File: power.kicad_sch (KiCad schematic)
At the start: 7 parts, among them J5 Conn_01x02, U1 MIC5365-2.8YC5

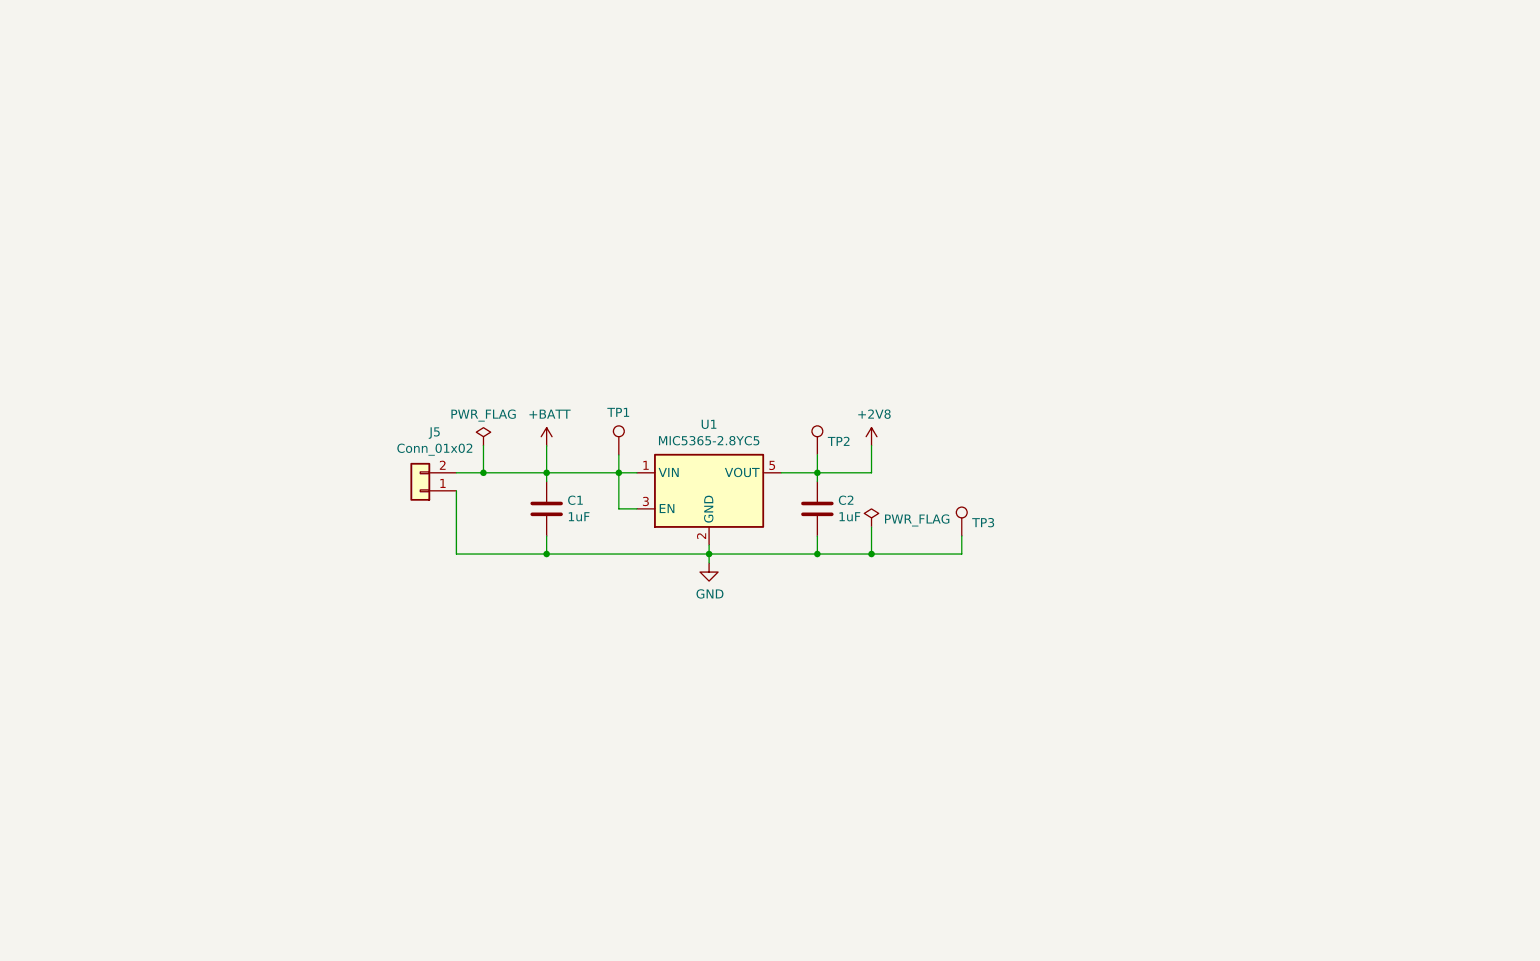
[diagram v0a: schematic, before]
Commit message: Initial schematic version
This is now a clean and ready version of the schematic:
That means:
- Schematic has been reviewed,
- It's fully annotated,
- All elements have been checked for availability with JLCPCB,
- Footprints were assigned,
- ERC is green.

No design changes should be added for this version until
the PCB is present and version is released.
Only bugfixes are possible now.
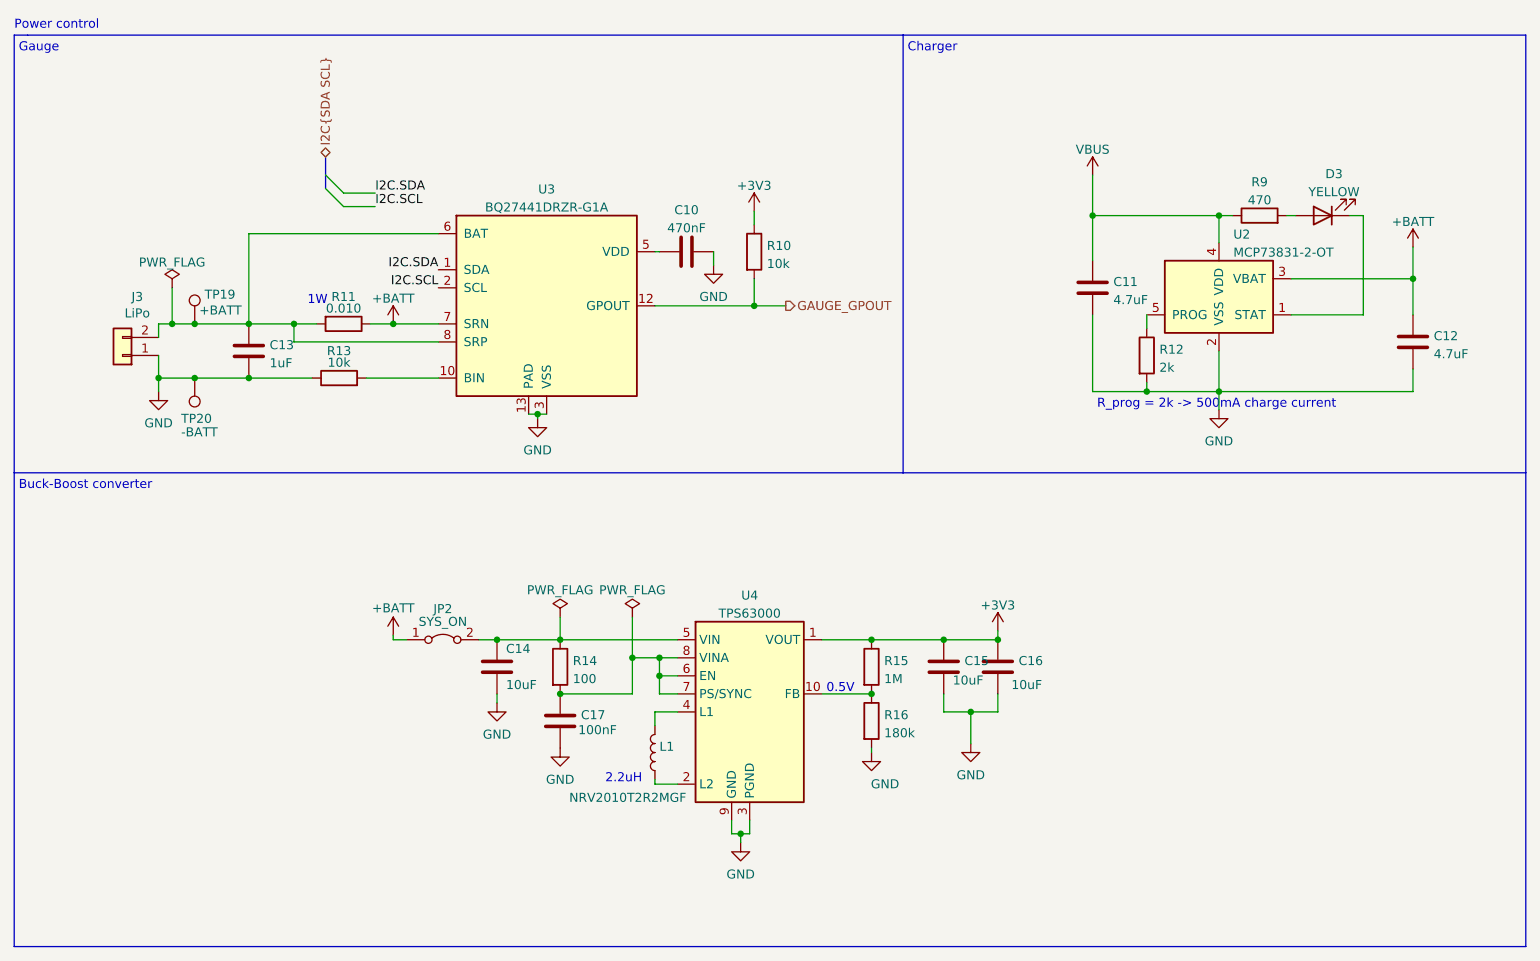
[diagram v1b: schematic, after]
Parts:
- removed C1, C2: 1uF, Capacitor_SMD:C_0402_1005Metric, symbol Device:C
- removed TP1, TP2, TP3: TestPoint, TestPoint:TestPoint_Pad_D2.0mm, symbol Connector:TestPoint
- removed U1: MIC5365-2.8YC5, Package_TO_SOT_SMD:SOT-353_SC-70-5, symbol cutomLDO:MIC5365-2.8YC5
- added C10: 470nF, Capacitor_SMD:C_0402_1005Metric, symbol Device:C
- added C11, C12: 4.7uF, Capacitor_SMD:C_0402_1005Metric, symbol Device:C
- added C13: 1uF, Capacitor_SMD:C_0402_1005Metric, symbol Device:C
- added C14, C15, C16: 10uF, Capacitor_SMD:C_0402_1005Metric, symbol Device:C
- added C17: 100nF, Capacitor_SMD:C_0402_1005Metric, symbol Device:C
- added D3: YELLOW, LED_SMD:LED_0402_1005Metric, symbol Device:LED
- added JP2: SYS_ON, Connector_PinHeader_2.54mm:PinHeader_1x02_P2.54mm_Vertical, symbol Jumper:Jumper_2_Bridged
- added L1: NRV2010T2R2MGF, Inductor_SMD:L_Taiyo-Yuden_NR-20xx, symbol Device:L
- added R10, R13: 10k, Resistor_SMD:R_0402_1005Metric, symbol Device:R
- added R11: 0.010, Resistor_SMD:R_2010_5025Metric, symbol Device:R
- added R12: 2k, Resistor_SMD:R_0402_1005Metric, symbol Device:R
- added R14: 100, Resistor_SMD:R_0402_1005Metric, symbol Device:R
- added R15: 1M, Resistor_SMD:R_0402_1005Metric, symbol Device:R
- added R16: 180k, Resistor_SMD:R_0402_1005Metric, symbol Device:R
- added R9: 470, Resistor_SMD:R_0402_1005Metric, symbol Device:R
- added TP19: +BATT, TestPoint:TestPoint_Pad_2.0x2.0mm, symbol Connector:TestPoint
- added TP20: -BATT, TestPoint:TestPoint_Pad_2.0x2.0mm, symbol Connector:TestPoint
- added U2: MCP73831-2-OT, Package_TO_SOT_SMD:SOT-23-5, symbol Battery_Management:MCP73831-2-OT
- added U3: BQ27441DRZR-G1A, Package_SON:Texas_S-PDSO-N12, symbol Battery_Management:BQ27441DRZR-G1A
- added U4: TPS63000, Package_SON:Texas_DRC0010J_ThermalVias, symbol Regulator_Switching:TPS63000
- J3: renamed from J5; value Conn_01x02 -> LiPo; footprint Connector_PinSocket_2.54mm:PinSocket_1x02_P2.54mm_Vertical -> Connector_PinHeader_2.54mm:PinHeader_1x02_P2.54mm_Vertical
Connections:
- net +BATT: now also C12.1, JP2.1 (A), R11.1, U2.3 (VBAT), U3.7 (SRN); no longer J3.2 (Pin_2)
- net GND: now also C10.2, C11.2, C12.2, C13.2, C14.2, C15.2, C16.2, C17.2, R12.2, R13.1, R16.2, TP20.1, U2.2 (VSS), U3.13 (PAD), U3.3 (VSS), U4.11 (PGND), U4.3 (PGND), U4.9 (GND)
- new net: C13.1, J3.2 (Pin_2), R11.2, TP19.1, U3.6 (BAT), U3.8 (SRP)
- new net: D3.2 (A), R9.2
- new net: L1.1, U4.2 (L2)
- new net: L1.2, U4.4 (L1)
- new net: C14.1, JP2.2 (B), R14.1, U4.5 (VIN)
- new net: C17.1, R14.2, U4.6 (EN), U4.7 (PS/SYNC), U4.8 (VINA)
- new net: R13.2, U3.10 (BIN)
- new net: D3.1 (K), U2.1 (STAT)
- new net: R12.1, U2.5 (PROG)
- new net: R15.2, R16.1, U4.10 (FB)
- new net: C10.1, U3.5 (VDD)
- new net +3V3: C15.1, C16.1, R10.1, R15.1, U4.1 (VOUT)
- new net GAUGE_GPOUT: R10.2, U3.12 (GPOUT)
- new net I2C.SCL: U3.2 (SCL)
- new net I2C.SDA: U3.1 (SDA)
- new net VBUS: C11.1, R9.1, U2.4 (VDD)
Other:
- note added: "0.5V"
- note added: "1W"
- note added: "2.2uH"
- note added: "Buck-Boost converter"
- note added: "Charger"
- note added: "Gauge"
- note added: "Power control"
- note added: "R_prog = 2k -> 500mA charge current"
- moved on the sheet: J3

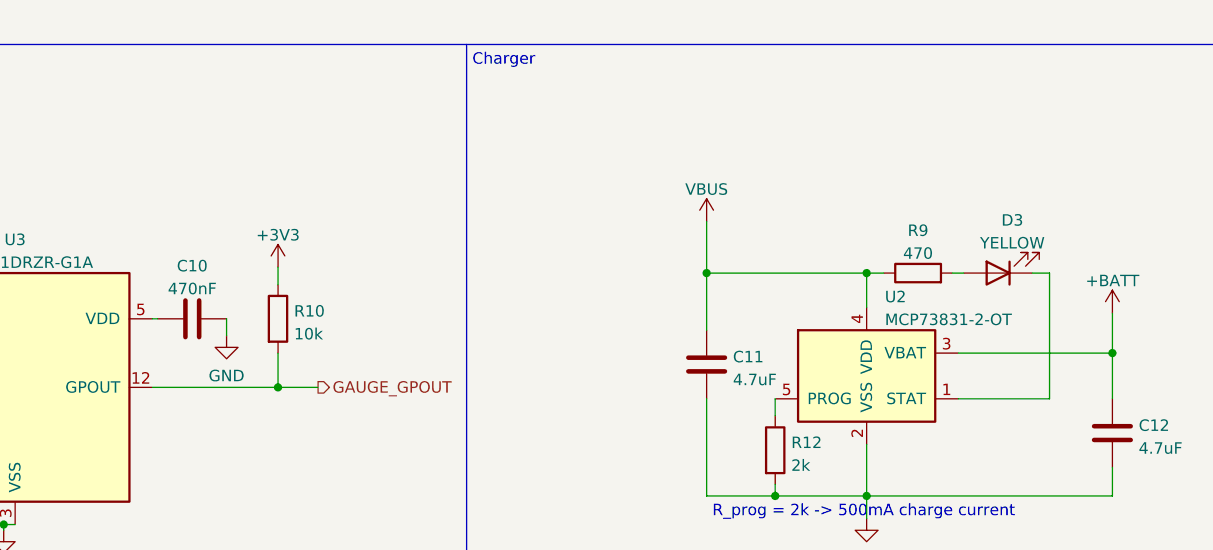
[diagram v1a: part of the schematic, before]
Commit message: Update footprints and add JLCPCB fields
Update some footprints which will suit better building the pcb
with JLCBPCB. Add fields to components sourced from JLCPCB
to be able to generate BOM.
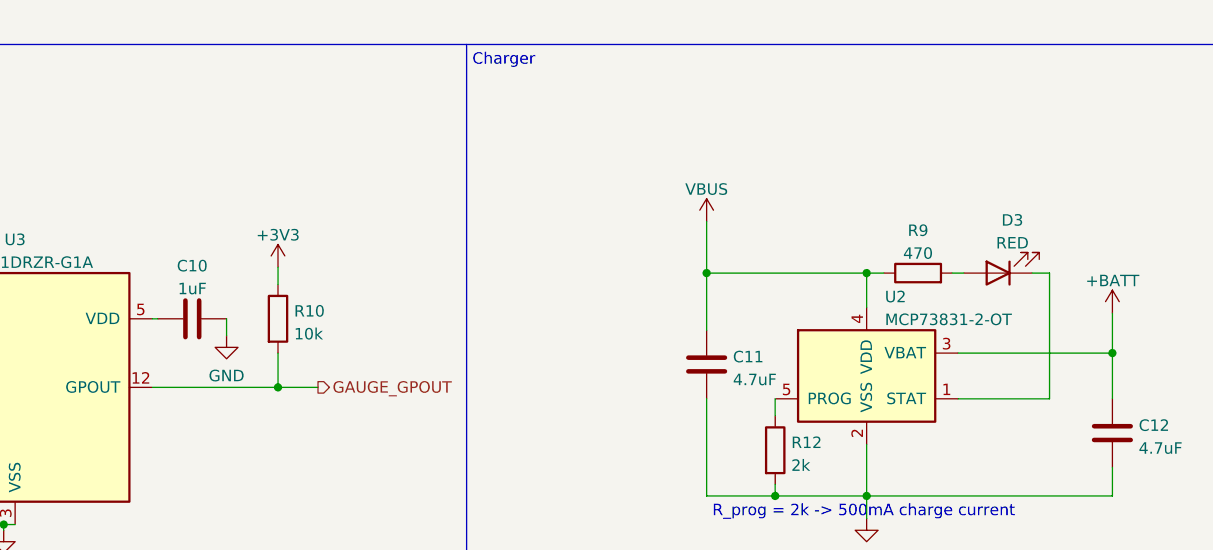
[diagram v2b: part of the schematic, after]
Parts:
- C10: value 470nF -> 1uF; JLC (none) -> 0402; LCSC (none) -> C52923
- C11, C12: JLC (none) -> 0402; LCSC (none) -> C23733
- C13: JLC (none) -> 0402; LCSC (none) -> C52923
- C14, C15, C16: JLC (none) -> 0402; LCSC (none) -> C15525
- C17: JLC (none) -> 0402; LCSC (none) -> C1525
- D3: value YELLOW -> RED; footprint LED_SMD:LED_0402_1005Metric -> LED_SMD:LED_0603_1608Metric; JLC (none) -> 0603; LCSC (none) -> C2286
- L1: JLC (none) -> SMD; LCSC (none) -> C222837
- R10, R13: JLC (none) -> 0402; LCSC (none) -> C25744
- R11: JLC (none) -> 2010; LCSC (none) -> C175965
- R12: JLC (none) -> 0402; LCSC (none) -> C4109
- R14: JLC (none) -> 0402; LCSC (none) -> C25076
- R15: JLC (none) -> 0402; LCSC (none) -> C26083
- R16: JLC (none) -> 0402; LCSC (none) -> C25760
- R9: JLC (none) -> 0402; LCSC (none) -> C25117
- U2: JLC (none) -> SOT-23-5; LCSC (none) -> C424093
- U3: JLC (none) -> SON-12-EP(2.5x4); LCSC (none) -> C473397
- U4: JLC (none) -> SON-10-EP(3.1x3.1); LCSC (none) -> C24966
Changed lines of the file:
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@@
+      (effects (font (size 1.27 1.27)) hide)
+    )
+    (property "JLC" "0402" (id 4) (at 209.55 57.785 0)
+      (effects (font (size 1.27 1.27)) hide)
+    )
+    (property "LCSC" "C25117" (id 5) (at 209.55 57.785 0)
       (effects (font (size 1.27 1.27)) hide)
     )
@@
       (effects (font (size 1.27 1.27)) hide)
     )
+    (property "JLC" "SMD" (id 4) (at 124.46 133.35 0)
+      (effects (font (size 1.27 1.27)) hide)
+    )
+    (property "LCSC" "C222837" (id 5) (at 124.46 133.35 0)
+      (effects (font (size 1.27 1.27)) hide)
+    )
     (pin "1")
     (pin "2")
@@
     )
     (property "Datasheet" "~" (id 3) (at 138.43 62.865 0)
+      (effects (font (size 1.27 1.27)) hide)
+    )
+    (property "JLC" "0402" (id 4) (at 138.43 62.865 0)
+      (effects (font (size 1.27 1.27)) hide)
+    )
+    (property "LCSC" " C25744" (id 5) (at 138.43 62.865 0)
       (effects (font (size 1.27 1.27)) hide)
     )
@@
       (effects (font (size 1.27 1.27)) hide)
     )
+    (property "JLC" "0402" (id 4) (at 111.125 121.285 0)
+      (effects (font (size 1.27 1.27)) hide)
+    )
+    (property "LCSC" " C25076" (id 5) (at 111.125 121.285 0)
+      (effects (font (size 1.27 1.27)) hide)
+    )
     (pin "1")
     (pin "2")
@@
     )
     (property "Datasheet" "~" (id 3) (at 67.31 76.835 0)
+      (effects (font (size 1.27 1.27)) hide)
+    )
+    (property "JLC" "0402" (id 4) (at 67.31 76.835 0)
+      (effects (font (size 1.27 1.27)) hide)
+    )
+    (property "LCSC" "C52923" (id 5) (at 67.31 76.835 0)
       (effects (font (size 1.27 1.27)) hide)
     )
@@
       (effects (font (size 1.27 1.27)) hide)
     )
+    (property "JLC" "0402" (id 4) (at 80.01 80.645 0)
+      (effects (font (size 1.27 1.27)) hide)
+    )
+    (property "LCSC" " C25744" (id 5) (at 80.01 80.645 0)
+      (effects (font (size 1.27 1.27)) hide)
+    )
     (pin "1")
     (pin "2")
@@
     )
     (property "Datasheet" "~" (id 3) (at 111.125 128.905 0)
+      (effects (font (size 1.27 1.27)) hide)
+    )
+    (property "JLC" "0402" (id 4) (at 111.125 128.905 0)
+      (effects (font (size 1.27 1.27)) hide)
+    )
+    (property "LCSC" "C1525" (id 5) (at 111.125 128.905 0)
       (effects (font (size 1.27 1.27)) hide)
     )
@@
       (effects (font (size 1.27 1.27)) hide)
     )
+    (property "JLC" "0402" (id 4) (at 172.72 121.285 0)
+      (effects (font (size 1.27 1.27)) hide)
+    )
+    (property "LCSC" "C15525" (id 5) (at 172.72 121.285 0)
+      (effects (font (size 1.27 1.27)) hide)
+    )
     (pin "1")
     (pin "2")
@@
     )
     (property "Datasheet" "~" (id 3) (at 102.235 121.285 0)
+      (effects (font (size 1.27 1.27)) hide)
+    )
+    (property "JLC" "0402" (id 4) (at 102.235 121.285 0)
+      (effects (font (size 1.27 1.27)) hide)
+    )
+    (property "LCSC" "C15525" (id 5) (at 102.235 121.285 0)
       (effects (font (size 1.27 1.27)) hide)
     )
@@
       (effects (font (size 1.27 1.27)) hide)
     )
+    (property "JLC" "SOT-23-5" (id 4) (at 203.835 69.215 0)
+      (effects (font (size 1.27 1.27)) hide)
+    )
+    (property "LCSC" "C424093" (id 5) (at 203.835 69.215 0)
+      (effects (font (size 1.27 1.27)) hide)
+    )
     (pin "1")
     (pin "2")
@@
       (effects (font (size 1.27 1.27)) hide)
     )
+    (property "JLC" "0402" (id 4) (at 186.055 67.945 0)
+      (effects (font (size 1.27 1.27)) hide)
+    )
+    (property "LCSC" "C23733" (id 5) (at 186.055 67.945 0)
+      (effects (font (size 1.27 1.27)) hide)
+    )
     (pin "1")
     (pin "2")
@@
       (effects (font (size 1.27 1.27)) hide)
     )
+    (property "JLC" "2010" (id 4) (at 80.645 73.025 0)
+      (effects (font (size 1.27 1.27)) hide)
+    )
+    (property "LCSC" "C175965" (id 5) (at 80.645 73.025 0)
+      (effects (font (size 1.27 1.27)) hide)
+    )
     (pin "1")
     (pin "2")
@@
     )
     (property "Datasheet" "~" (id 3) (at 154.94 121.285 0)
+      (effects (font (size 1.27 1.27)) hide)
+    )
+    (property "JLC" "0402" (id 4) (at 154.94 121.285 0)
+      (effects (font (size 1.27 1.27)) hide)
+    )
+    (property "LCSC" "C26083" (id 5) (at 154.94 121.285 0)
       (effects (font (size 1.27 1.27)) hide)
     )
@@
     (in_bom yes) (on_board yes) (fields_autoplaced)
     (property "Reference" "C10" (id 0) (at 128.905 57.0062 90))
-    (property "Value" "470nF" (id 1) (at 128.905 59.5431 90))
+    (property "Value" "1uF" (id 1) (at 128.905 59.5431 90))
     (property "Footprint" "Capacitor_SMD:C_0402_1005Metric" (id 2) (at 132.715 61.8998 0)
       (effects (font (size 1.27 1.27)) hide)
@@
       (effects (font (size 1.27 1.27)) hide)
     )
+    (property "JLC" "0402" (id 4) (at 128.905 62.865 0)
+      (effects (font (size 1.27 1.27)) hide)
+    )
+    (property "LCSC" "C52923" (id 5) (at 128.905 62.865 0)
+      (effects (font (size 1.27 1.27)) hide)
+    )
     (pin "1")
     (pin "2")
@@
     )
     (property "Datasheet" "~" (id 3) (at 154.94 128.905 0)
+      (effects (font (size 1.27 1.27)) hide)
+    )
+    (property "JLC" "0402" (id 4) (at 154.94 128.905 0)
+      (effects (font (size 1.27 1.27)) hide)
+    )
+    (property "LCSC" " C25760 " (id 5) (at 154.94 128.905 0)
       (effects (font (size 1.27 1.27)) hide)
     )
@@
     )
     (property "Datasheet" "http://www.ti.com/lit/ds/symlink/tps63000.pdf" (id 3) (at 130.175 113.665 0)
+      (effects (font (size 1.27 1.27)) hide)
+    )
+    (property "JLC" "SON-10-EP(3.1x3.1)" (id 4) (at 137.795 127.635 0)
+      (effects (font (size 1.27 1.27)) hide)
+    )
+    (property "LCSC" "C24966" (id 5) (at 137.795 127.635 0)
       (effects (font (size 1.27 1.27)) hide)
     )
@@
       (effects (font (size 1.27 1.27)) hide)
     )
+    (property "JLC" "0402" (id 4) (at 193.675 77.47 0)
+      (effects (font (size 1.27 1.27)) hide)
+    )
+    (property "LCSC" "C4109" (id 5) (at 193.675 77.47 0)
+      (effects (font (size 1.27 1.27)) hide)
+    )
     (pin "1")
     (pin "2")
@@
     (in_bom yes) (on_board yes) (fields_autoplaced)
     (property "Reference" "D3" (id 0) (at 220.0275 51.9262 0))
-    (property "Value" "YELLOW" (id 1) (at 220.0275 54.4631 0))
-    (property "Footprint" "LED_SMD:LED_0402_1005Metric" (id 2) (at 218.44 57.785 0)
+    (property "Value" "RED" (id 1) (at 220.0275 54.4631 0))
+    (property "Footprint" "LED_SMD:LED_0603_1608Metric" (id 2) (at 218.44 57.785 0)
       (effects (font (size 1.27 1.27)) hide)
     )
     (property "Datasheet" "~" (id 3) (at 218.44 57.785 0)
+      (effects (font (size 1.27 1.27)) hide)
+    )
+    (property "JLC" "0603" (id 4) (at 218.44 57.785 0)
+      (effects (font (size 1.27 1.27)) hide)
+    )
+    (property "LCSC" "C2286" (id 5) (at 218.44 57.785 0)
       (effects (font (size 1.27 1.27)) hide)
     )
@@
       (effects (font (size 1.27 1.27)) hide)
     )
+    (property "JLC" "0402" (id 4) (at 231.14 75.565 0)
+      (effects (font (size 1.27 1.27)) hide)
+    )
+    (property "LCSC" "C23733" (id 5) (at 231.14 75.565 0)
+      (effects (font (size 1.27 1.27)) hide)
+    )
     (pin "1")
     (pin "2")
@@
     )
     (property "Datasheet" "~" (id 3) (at 165.1 121.285 0)
+      (effects (font (size 1.27 1.27)) hide)
+    )
+    (property "JLC" "0402" (id 4) (at 165.1 121.285 0)
+      (effects (font (size 1.27 1.27)) hide)
+    )
+    (property "LCSC" "C15525" (id 5) (at 165.1 121.285 0)
       (effects (font (size 1.27 1.27)) hide)
     )
@@
       (effects (font (size 1.27 1.27)) hide)
     )
+    (property "JLC" "SON-12-EP(2.5x4)" (id 4) (at 109.22 70.485 0)
+      (effects (font (size 1.27 1.27)) hide)
+    )
+    (property "LCSC" "C473397" (id 5) (at 109.22 70.485 0)
+      (effects (font (size 1.27 1.27)) hide)
+    )
